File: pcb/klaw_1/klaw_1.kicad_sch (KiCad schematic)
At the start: 70 parts, among them J1 PJ-320A-4P, J3 lv27, SW1 SW_PUSH-MX_W_LED, SW10 SW_PUSH-MX_W_LED, SW12 SW_PUSH-MX_W_LED, SW13 SW_PUSH-MX_W_LED, SW14 SW_PUSH-MX_W_LED, SW15 SW_PUSH-MX_W_LED, SW16 SW_PUSH-MX_W_LED, SW18 EC11N1525404, SW2 SW_PUSH-MX_W_LED, SW20 SW_PUSH-MX_W_LED, SW21 SW_PUSH-MX_W_LED, SW3 SW_PUSH-MX_W_LED, SW4 SW_PUSH-MX_W_LED, SW5 SW_PUSH-MX_W_LED, SW6 SW_PUSH-MX_W_LED, SW7 SW_PUSH-MX_W_LED, SW8 SW_PUSH-MX_W_LED, SW9 SW_PUSH-MX_W_LED, U1 ProMicro

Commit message: refactor: rename KLOR* libraries to klaw*
- KLOR.pretty -> klaw.pretty, KLOR.3dshapes -> klaw.3dshapes,
  KLORlib.kicad_sym -> klawlib.kicad_sym
- lib nicknames, footprint ids, lib_ids, model paths, and doc
  references updated throughout; netlist verified identical and
  all footprints/symbols resolve (zero lib issues)
- prose credits to the KLOR project unchanged
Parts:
- BT1: footprint KLOR:JST_PH_reversible -> klaw:JST_PH_reversible; symbol KLORlib:Battery_Cell -> klawlib:Battery_Cell
- BT2: footprint KLOR:custombatteryconnector_small -> klaw:custombatteryconnector_small; symbol KLORlib:Battery_Cell -> klawlib:Battery_Cell
- BZ1: footprint KLOR:Buzzer_Mallory_AST1109MLTRQ_reversible -> klaw:Buzzer_Mallory_AST1109MLTRQ_reversible; symbol KLORlib:Buzzer -> klawlib:Buzzer
- D1, D10, D12, D13, D14, D15, D16, D18, D2, D20, D21, D3, D4, D5, D6, D7, D8, D9: footprint KLOR:Diode_SOD123 -> klaw:Diode_SOD123; symbol KLORlib:D_Small -> klawlib:D_Small
- J1: footprint KLOR:MJ-4PP-9 -> klaw:MJ-4PP-9; symbol KLORlib:MJ-4PP-9 TRRS -> klawlib:MJ-4PP-9 TRRS
- J3: footprint KLOR:lvc27_onlyInput -> klaw:lvc27_onlyInput; symbol KLORlib:Conn_01x05 -> klawlib:Conn_01x05
- JP1, JP16, JP17, JP18, JP19, JP2, JP20, JP21, JP22, JP23, JP24, JP25, JP3, JP4, JP5, JP6, JP7, JP8: footprint KLOR:R_0603_1608Metric -> klaw:R_0603_1608Metric; symbol KLORlib:R_0R -> klawlib:R_0R
- MH1, MH2, MH3, MH5, MH6, MH7, MH8: footprint KLOR:MountingHole_3.2mm_M3 -> klaw:MountingHole_3.2mm_M3; symbol KLORlib:MountingHole -> klawlib:MountingHole
- OLED1: footprint KLOR:SSD1306_128x64OLED -> klaw:SSD1306_128x64OLED; symbol KLORlib:SSD1306 -> klawlib:SSD1306
- PSW1: footprint KLOR:MSK12C02_reversible -> klaw:MSK12C02_reversible; symbol KLORlib:SW_DPDT_x2 -> klawlib:SW_DPDT_x2
- RSW1: footprint KLOR:SW_Push_1P1T-MP_NO_Horizontal_Alps_SKRTLAE010_both_sides -> klaw:SW_Push_1P1T-MP_NO_Horizontal_Alps_SKRTLAE010_both_sides; symbol KLORlib:SW_Push -> klawlib:SW_Push
- SW1, SW10, SW12, SW13, SW14, SW15, SW16, SW2, SW20, SW21, SW3, SW4, SW5, SW6, SW7, SW8, SW9: footprint KLOR:SK6812MINI_and_cherry -> klaw:SK6812MINI_and_cherry; symbol KLORlib:SW_PUSH-MX_W_LED -> klawlib:SW_PUSH-MX_W_LED
- SW18: footprint KLOR:RotaryEncoder_Alps_EC11E-Switch_Vertical_H20mm-keebio_modified -> klaw:RotaryEncoder_Alps_EC11E-Switch_Vertical_H20mm-keebio_modified; symbol KLORlib:RotaryEncoder_Switch -> klawlib:RotaryEncoder_Switch
- U1: footprint KLOR:ProMicro -> klaw:ProMicro; symbol KLORlib:ProMicro -> klawlib:ProMicro

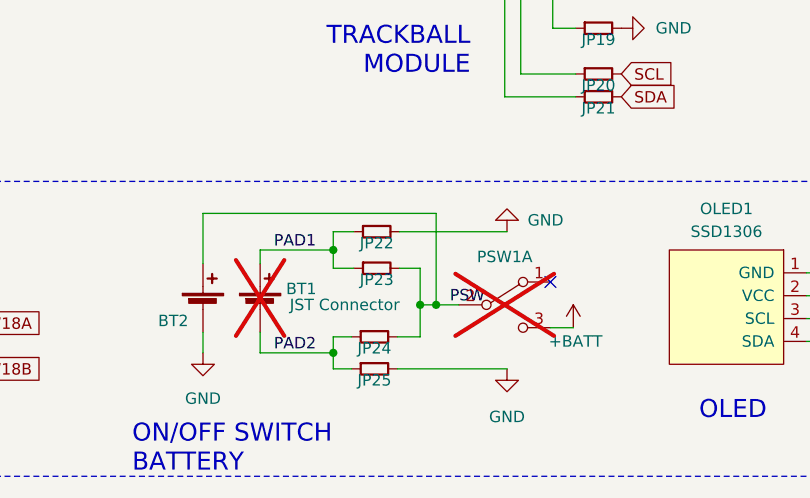
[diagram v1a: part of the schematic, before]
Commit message: feat: power switch rework per datasheet + board fixes; prod refresh
- PSW1 ON-throw moved to pin 1 per MSK12C02 datasheet; shared pin
  numbering across faces makes DRC enforce the mirrored feed for
  both builds (verified: 0 unconnected, parity clean)
- GND stitches restored after case-fit moves; stale rev-1 track
  deleted for good
- fresh gerbers (case-fit positions, resistor silk, PSW rework);
  CPLs verified against unmoved assembly positions
- doc renders refreshed
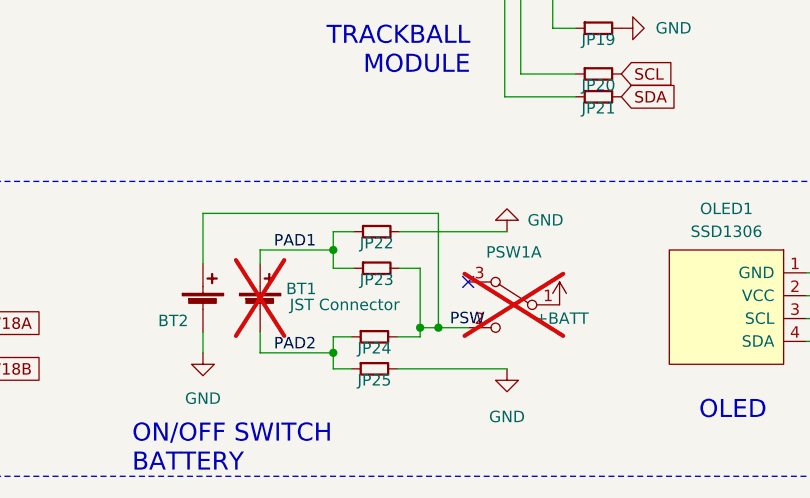
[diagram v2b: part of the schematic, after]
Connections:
- net +BATT: now also PSW1.1 (B); no longer PSW1.3 (C)
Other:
- moved on the sheet: PSW1A
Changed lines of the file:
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@@
 	)
 	(junction
+		(at 105.41 178.562)
+		(diameter 0)
+		(color 0 0 0 0)
+	)
+	(junction
 		(at 218.948 67.056)
 		(diameter 0)
@@
 	)
 	(junction
-		(at 107.188 176.022)
-		(diameter 0)
-		(color 0 0 0 0)
-	)
-	(junction
 		(at 95.758 169.926)
 		(diameter 0)
@@
 	)
 	(junction
+		(at 107.442 178.562)
+		(diameter 0)
+		(color 0 0 0 0)
+	)
+	(junction
 		(at 229.108 133.858)
 		(diameter 0)
@@
 	)
 	(junction
-		(at 105.41 176.022)
-		(diameter 0)
-		(color 0 0 0 0)
-	)
-	(junction
 		(at 242.57 133.858)
 		(diameter 0)
@@
 	)
 	(no_connect
-		(at 119.888 173.482)
+		(at 110.744 173.482)
 	)
 	(no_connect
@@
 	(wire
 		(pts
-			(xy 105.41 176.022) (xy 105.41 179.578)
+			(xy 105.41 171.958) (xy 105.41 178.562)
 		)
 		(stroke
@@
 	(wire
 		(pts
-			(xy 105.41 176.022) (xy 107.188 176.022)
+			(xy 105.41 178.562) (xy 107.442 178.562)
 		)
 		(stroke
@@
 	(wire
 		(pts
-			(xy 105.41 171.958) (xy 105.41 176.022)
-		)
-		(stroke
-			(width 0)
-			(type default)
-		)
-	)
-	(wire
-		(pts
 			(xy 149.352 180.086) (xy 154.432 180.086)
 		)
@@
 	(wire
 		(pts
-			(xy 119.888 178.562) (xy 122.428 178.562)
+			(xy 95.758 179.578) (xy 97.79 179.578)
 		)
 		(stroke
@@
 	(wire
 		(pts
-			(xy 95.758 179.578) (xy 97.79 179.578)
+			(xy 204.47 127.762) (xy 204.47 133.858)
 		)
 		(stroke
@@
 	(wire
 		(pts
-			(xy 204.47 127.762) (xy 204.47 133.858)
+			(xy 201.168 39.116) (xy 201.168 53.086)
 		)
 		(stroke
@@
 	(wire
 		(pts
-			(xy 201.168 39.116) (xy 201.168 53.086)
+			(xy 221.488 72.136) (xy 239.268 72.136)
 		)
 		(stroke
@@
 	(wire
 		(pts
-			(xy 221.488 72.136) (xy 239.268 72.136)
+			(xy 241.046 122.682) (xy 242.57 122.682)
 		)
 		(stroke
@@
 	(wire
 		(pts
-			(xy 241.046 122.682) (xy 242.57 122.682)
+			(xy 116.586 136.398) (xy 116.586 150.368)
 		)
 		(stroke
@@
 	(wire
 		(pts
-			(xy 116.586 136.398) (xy 116.586 150.368)
+			(xy 105.41 178.562) (xy 105.41 179.578)
 		)
 		(stroke
@@
 	(wire
 		(pts
-			(xy 107.188 176.022) (xy 109.728 176.022)
+			(xy 107.442 178.562) (xy 110.744 178.562)
 		)
 		(stroke
@@
 	(wire
 		(pts
-			(xy 107.188 165.862) (xy 107.188 176.022)
+			(xy 107.442 165.862) (xy 107.442 178.562)
 		)
 		(stroke
@@
 	(wire
 		(pts
-			(xy 81.28 165.862) (xy 107.188 165.862)
+			(xy 81.28 165.862) (xy 107.442 165.862)
 		)
 		(stroke
@@
 	)
 	(label "PSW"
-		(at 108.712 176.022 0)
+		(at 108.712 178.562 0)
 		(effects
 			(font
@@
 	(symbol
 		(lib_id "klawlib:SW_DPDT_x2")
-		(at 114.808 176.022 0)
+		(at 115.824 176.022 0)
+		(mirror y)
 		(unit 1)
 		(body_style 1)
@@
 		(in_pos_files yes)
 		(dnp yes)
-		(fields_autoplaced yes)
 		(property "Reference" "PSW1"
-			(at 114.808 170.688 0)
+			(at 115.824 170.18 0)
 			(show_name no)
 			(do_not_autoplace no)
@@
 		)
 		(property "Value" "SW_DPDT_x2"
-			(at 114.808 170.942 0)
+			(at 115.824 170.942 0)
 			(hide yes)
 			(show_name no)
@@
 		)
 		(property "Footprint" "klaw:MSK12C02_reversible"
-			(at 114.808 176.022 0)
+			(at 115.824 176.022 0)
 			(hide yes)
 			(show_name no)
@@
 		)
 		(property "Datasheet" ""
-			(at 114.808 176.022 0)
+			(at 115.824 176.022 0)
 			(hide yes)
 			(show_name no)
@@
 			)
 		)
-		(property "Description" ""
-			(at 114.808 176.022 0)
+		(property "Description" "Switch, dual pole double throw, separate symbols"
+			(at 115.824 176.022 0)
+			(hide yes)
 			(show_name no)
 			(do_not_autoplace no)
@@
 		)
 		(property "LCSC" "C431540"
-			(at 114.808 176.022 0)
+			(at 115.824 176.022 0)
 			(hide yes)
 			(show_name no)
@@
 		)
 		(property "Price" "0.0540@10"
-			(at 114.808 176.022 0)
+			(at 115.824 176.022 0)
 			(hide yes)
 			(show_name no)
@@
 		)
 		(property "Stock" "164580"
-			(at 114.808 176.022 0)
+			(at 115.824 176.022 0)
 			(hide yes)
 			(show_name no)
@@
 		)
 		(property "Checked" "2026-08-20"
-			(at 114.808 176.022 0)
+			(at 115.824 176.022 0)
 			(hide yes)
 			(show_name no)
@@
 		)
 		(property "Assembly" "JLC"
-			(at 114.808 176.022 0)
+			(at 115.824 176.022 0)
 			(hide yes)
 			(show_name no)
@@
 	(symbol
 		(lib_id "power:+BATT")
-		(at 122.428 178.562 0)
+		(at 120.904 176.022 0)
 		(unit 1)
 		(body_style 1)
@@
 		(dnp no)
 		(property "Reference" "#PWR0104"
-			(at 122.428 182.372 0)
+			(at 120.904 179.832 0)
 			(hide yes)
 			(show_name no)
@@
 		)
 		(property "Value" "+BATT"
-			(at 122.682 180.086 0)
+			(at 121.158 177.546 0)
 			(show_name no)
 			(do_not_autoplace no)
@@
 		)
 		(property "Footprint" ""
-			(at 122.428 178.562 0)
+			(at 120.904 176.022 0)
 			(hide yes)
 			(show_name no)
@@
 		)
 		(property "Datasheet" ""
-			(at 122.428 178.562 0)
+			(at 120.904 176.022 0)
 			(hide yes)
 			(show_name no)
@@
 		)
 		(property "Description" ""
-			(at 122.428 178.562 0)
+			(at 120.904 176.022 0)
 			(show_name no)
 			(do_not_autoplace no)
